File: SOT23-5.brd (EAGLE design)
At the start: 62.2 x 10.2 mm, 14 parts, among them J1 1X03, J2 1X03, J3 1X03, J4 1X03, J5 1X03, J6 1X03, J7 1X03, U1 SOT23-3, U2 SOT23-3, U3 SOT23-3, U4 SOT23-3, U5 SOT23-3, U6 SOT23-3, U7 SOT23-3

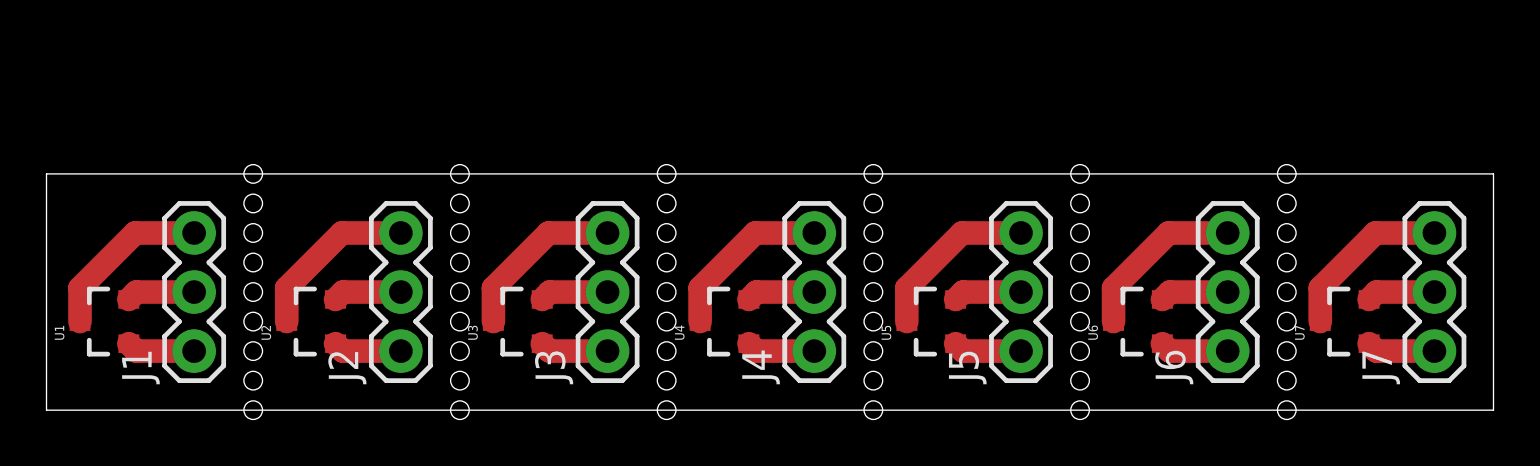
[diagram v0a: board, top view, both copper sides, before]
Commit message: Added an SOT23-5 breakout.
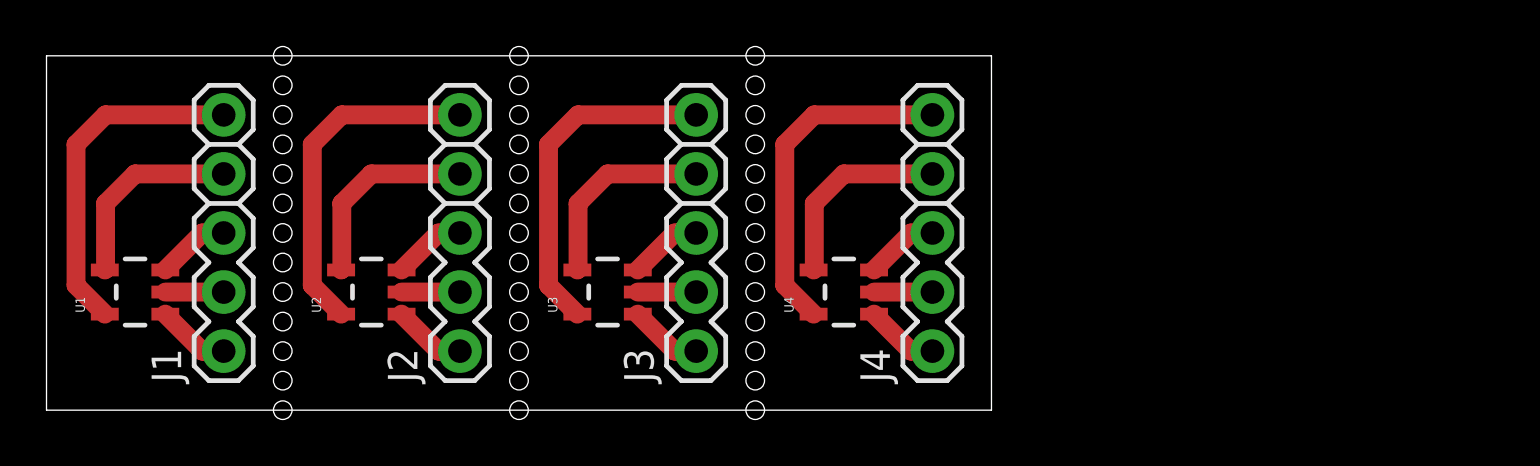
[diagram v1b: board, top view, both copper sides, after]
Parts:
- removed J5, J6, J7: 1X03, breakouts:1X03
- removed U5, U6, U7: SOT23-3, breakouts:SOT23-3
- J1, J2, J3, J4: value 1X03 -> 1X05; device breakouts:1X03 -> breakouts:1X05
- U1, U2, U3, U4: value SOT23-3 -> SOT23-5; device breakouts:SOT23-3 -> breakouts:SOT23-5
- moved U4 5.24 mm to (34.3, 5.08)
- moved J4 5.08 mm to (38.1, 2.54)
- moved U3 4.02 mm to (24.1, 5.08)
- moved J3 3.81 mm to (27.9, 2.54)
- moved U2 2.84 mm to (14.0, 5.08)
- moved J2 2.54 mm to (17.8, 2.54)
- moved U1 1.80 mm to (3.81, 5.08)
- moved J1 1.27 mm to (7.62, 2.54)
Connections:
- removed net N$13: J5.1, U5.1
- removed net N$14: J5.2, U5.2
- removed net N$15: J5.3, U5.3
- removed net N$16: J6.1, U6.1
- removed net N$17: J6.2, U6.2
- removed net N$18: J6.3, U6.3
- removed net N$19: J7.1, U7.1
- removed net N$20: J7.2, U7.2
- removed net N$21: J7.3, U7.3
- new net N$22: J1.4, U1.4
- new net N$23: J1.5, U1.5
- new net N$24: J2.4, U2.4
- new net N$25: J2.5, U2.5
- new net N$26: J3.4, U3.4
- new net N$27: J3.5, U3.5
- new net N$28: J4.4, U4.4
- new net N$29: J4.5, U4.5
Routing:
- net N$27: track 0.00 -> 14.7 mm
- net N$25: track 0.00 -> 14.7 mm
- net N$29: track 0.00 -> 14.7 mm
- net N$23: track 0.00 -> 14.7 mm
- net N$28: track 0.00 -> 8.48 mm
- net N$26: track 0.00 -> 8.48 mm
- net N$24: track 0.00 -> 8.48 mm
- net N$22: track 0.00 -> 8.48 mm
- net N$21: track 7.33 -> 0.00 mm
- net N$18: track 7.33 -> 0.00 mm
- net N$15: track 7.33 -> 0.00 mm
- net N$12: track 7.33 -> 3.17 mm
- net N$3: track 7.33 -> 3.17 mm
- net N$9: track 7.33 -> 3.17 mm
- net N$6: track 7.33 -> 3.17 mm
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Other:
- board size 62.2 x 10.2 mm -> 40.6 x 15.2 mm
- board text added: "4"
- board text added: "5"
- board text added: "SOT23-5"
- board text removed: "SOT23-3"

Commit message: Fix some silk screen flaws in pin header devices.
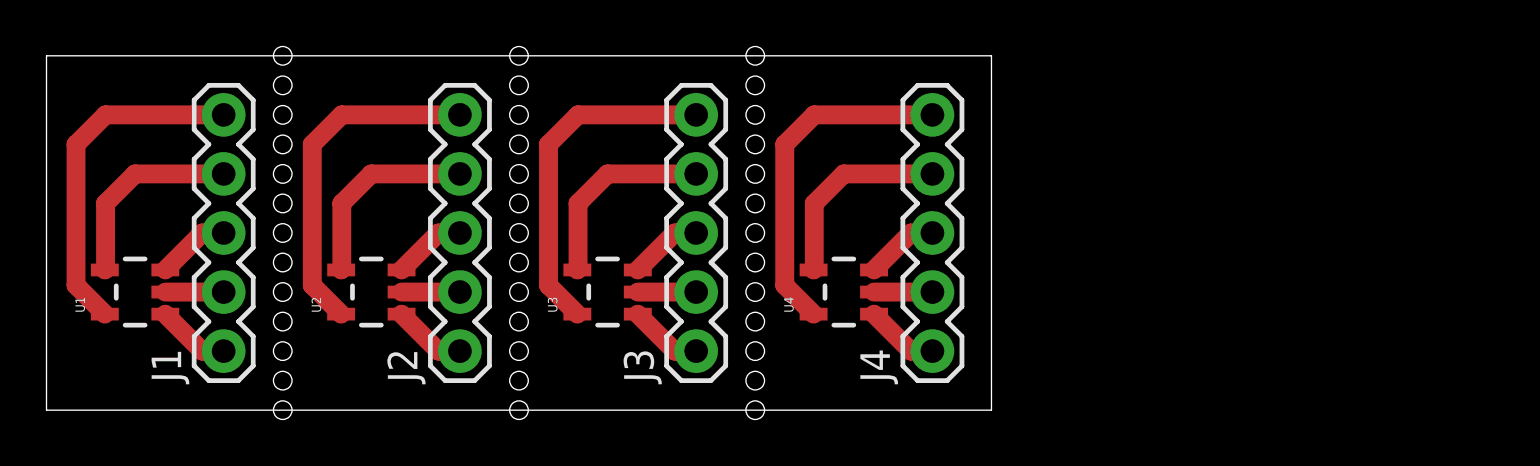
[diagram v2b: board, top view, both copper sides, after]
